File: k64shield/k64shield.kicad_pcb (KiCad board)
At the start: 2 copper layers, 7 parts, among them J1 top_left_header_02x08, J2 bottom_left_header_02x06, J3 rpi_motor_driver_header, J4 top_right_header_02x10, J5 bottom_right_header_02x08, J6 camera_header_01x05, J7 servo_header_01x03

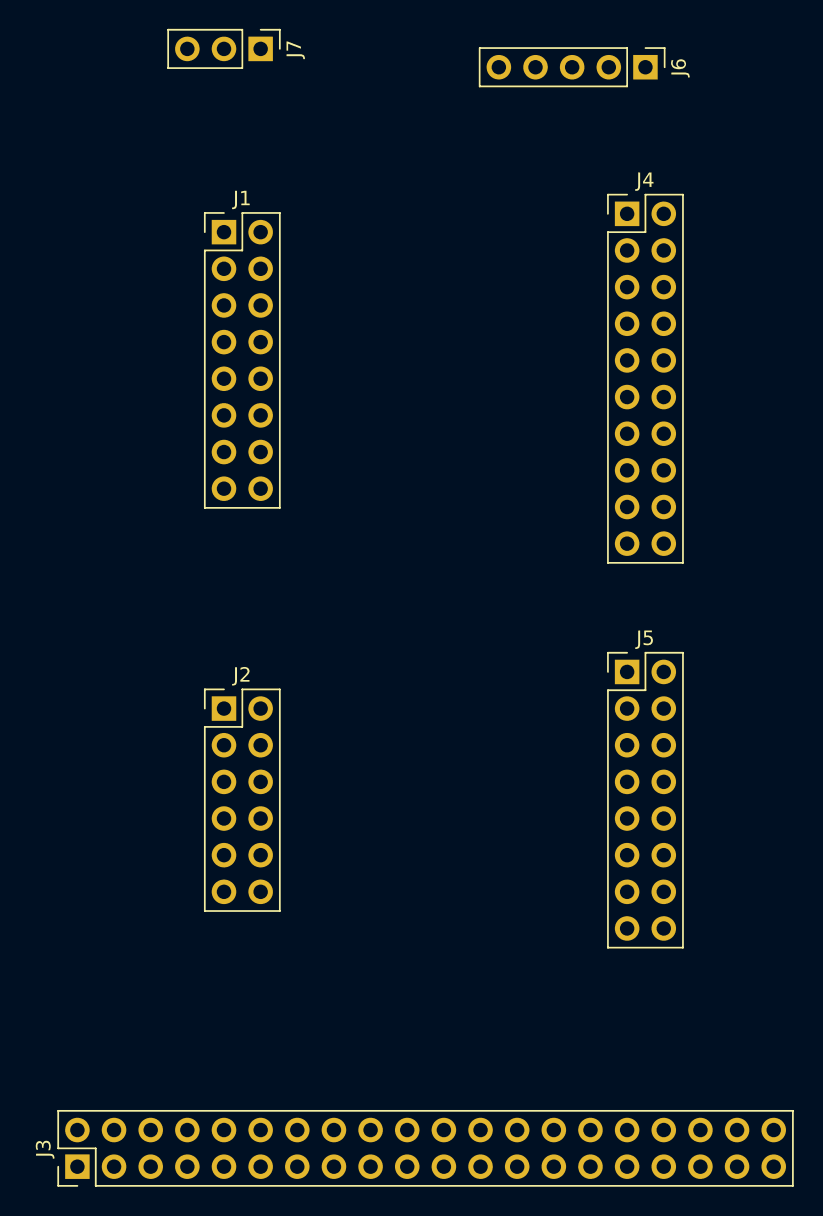
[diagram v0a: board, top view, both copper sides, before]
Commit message: Some of the PCB completed
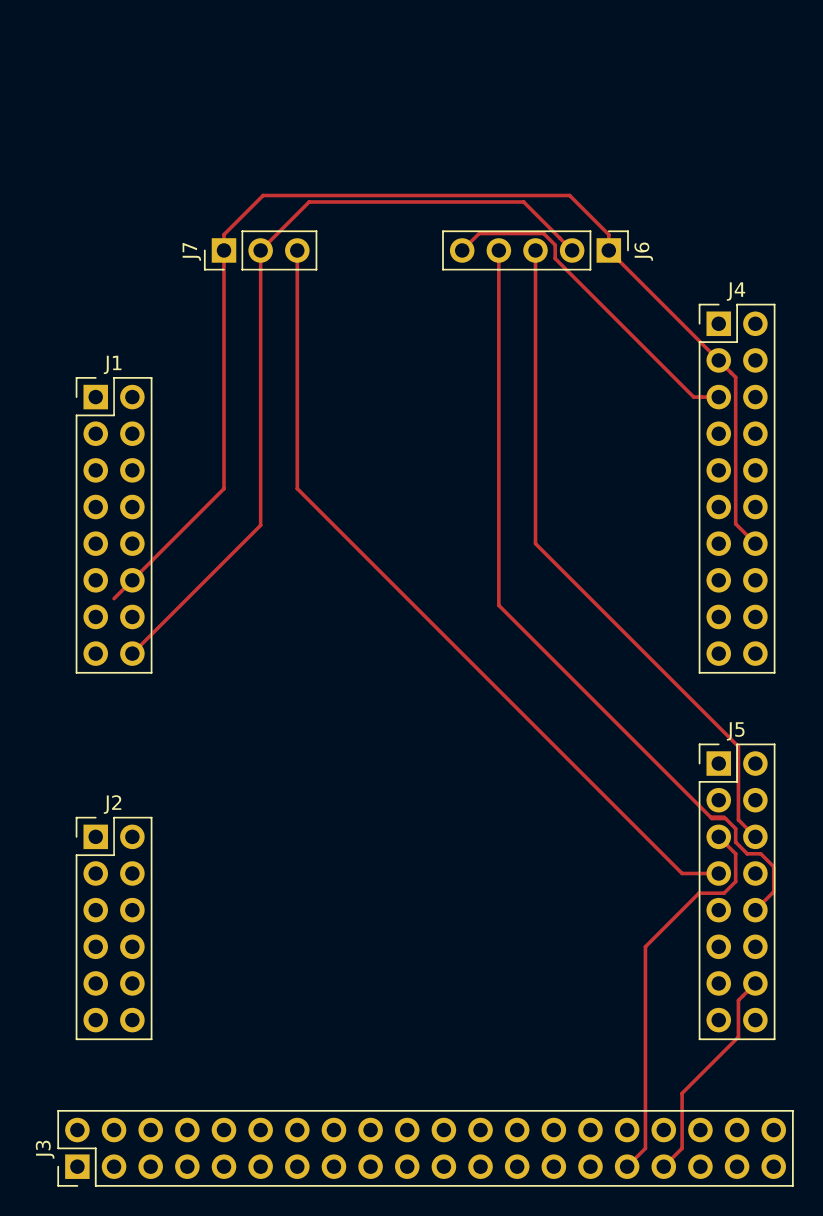
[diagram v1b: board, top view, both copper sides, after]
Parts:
- moved J1 14.5 mm to (104.1, 72.4)
- moved J7 14.2 mm to (113.0, 62.2), turned to 90 degrees
- moved J6 13.0 mm to (139.7, 62.2)
- moved J2 12.6 mm to (104.1, 102.9)
- moved J4 9.92 mm to (147.3, 67.3)
- moved J5 8.98 mm to (147.3, 97.8)
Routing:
- net /GND: track 0.00 -> 82.9 mm
- net /SIG: track 0.00 -> 56.8 mm
- net /SI: track 0.00 -> 56.2 mm
- net /5V: track 0.00 -> 56.0 mm
- net /CLK: track 0.00 -> 47.0 mm
- net /A1: track 0.00 -> 27.5 mm
- net /AO: track 0.00 -> 23.5 mm
- net /A2: track 0.00 -> 15.3 mm
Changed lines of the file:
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@@
-(kicad_pcb (version 4) (host pcbnew 4.0.7)
+(kicad_pcb (version 20171130) (host pcbnew 5.0.1-33cea8e~68~ubuntu18.04.1)
   (general
-    (links 25)
-    (no_connects 25)
-    (area 0 0 0 0)
     (thickness 1.6)
     (drawings 0)
-    (tracks 0)
+    (tracks 57)
     (zones 0)
     (modules 7)
@@
     (pad_drill 0.762)
     (pad_to_mask_clearance 0.2)
+    (solder_mask_min_width 0.25)
     (aux_axis_origin 0 0)
     (visible_elements FFFFFF7F)
@@
       (layerselection 0x00030_80000001)
       (usegerberextensions false)
+      (usegerberattributes false)
+      (usegerberadvancedattributes false)
+      (creategerberjobfile false)
       (excludeedgelayer true)
       (linewidth 0.100000)
@@
       (hpglpennumber 1)
       (hpglpenspeed 20)
-      (hpglpendiameter 15)
-      (hpglpenoverlay 2)
+      (hpglpendiameter 15.000000)
       (psnegative false)
       (psa4output false)
@@
   )
   (module Pin_Headers:Pin_Header_Straight_2x08_Pitch2.54mm (layer F.Cu)
-    (at 113.03 60.96)
+    (at 104.14 72.39)
     (descr "Through hole straight pin header, 2x08, 2.54mm pitch, double rows")
     (tags "Through hole pin header THT 2x08 2.54mm double row")
@@
   )
   (module Pin_Headers:Pin_Header_Straight_2x06_Pitch2.54mm (layer F.Cu)
-    (at 113.03 93.98)
+    (at 104.14 102.87)
     (descr "Through hole straight pin header, 2x06, 2.54mm pitch, double rows")
     (tags "Through hole pin header THT 2x06 2.54mm double row")
@@
   )
   (module Pin_Headers:Pin_Header_Straight_2x10_Pitch2.54mm (layer F.Cu)
-    (at 140.97 59.69)
+    (at 147.32 67.31)
     (descr "Through hole straight pin header, 2x10, 2.54mm pitch, double rows")
     (tags "Through hole pin header THT 2x10 2.54mm double row")
@@
   )
   (module Pin_Headers:Pin_Header_Straight_2x08_Pitch2.54mm (layer F.Cu)
-    (at 140.97 91.44)
+    (at 147.32 97.79)
     (descr "Through hole straight pin header, 2x08, 2.54mm pitch, double rows")
     (tags "Through hole pin header THT 2x08 2.54mm double row")
@@
   )
   (module Pin_Headers:Pin_Header_Straight_1x05_Pitch2.54mm (layer F.Cu)
-    (at 142.24 49.53 270)
+    (at 139.7 62.23 270)
     (descr "Through hole straight pin header, 1x05, 2.54mm pitch, single row")
     (tags "Through hole pin header THT 1x05 2.54mm single row")
@@
     (fp_line (start 1.8 11.95) (end 1.8 -1.8) (layer F.CrtYd) (width 0.05))
     (fp_line (start 1.8 -1.8) (end -1.8 -1.8) (layer F.CrtYd) (width 0.05))
-    (fp_text user %R (at 0 5.08 360) (layer F.Fab)
+    (fp_text user %R (at 0 5.08) (layer F.Fab)
       (effects (font (size 1 1) (thickness 0.15)))
     )
@@
   )
   (module Pin_Headers:Pin_Header_Straight_1x03_Pitch2.54mm (layer F.Cu)
-    (at 115.57 48.26 270)
+    (at 113.03 62.23 90)
     (descr "Through hole straight pin header, 1x03, 2.54mm pitch, single row")
     (tags "Through hole pin header THT 1x03 2.54mm single row")
-    (fp_text reference J7 (at 0 -2.33 270) (layer F.SilkS)
-      (effects (font (size 1 1) (thickness 0.15)))
-    )
-    (fp_text value servo_header_01x03 (at 0 7.41 270) (layer F.Fab)
+    (fp_text reference J7 (at 0 -2.33 90) (layer F.SilkS)
+      (effects (font (size 1 1) (thickness 0.15)))
+    )
+    (fp_text value servo_header_01x03 (at 0 7.41 90) (layer F.Fab)
       (effects (font (size 1 1) (thickness 0.15)))
     )
@@
     (fp_line (start 1.8 6.85) (end 1.8 -1.8) (layer F.CrtYd) (width 0.05))
     (fp_line (start 1.8 -1.8) (end -1.8 -1.8) (layer F.CrtYd) (width 0.05))
-    (fp_text user %R (at 0 2.54 360) (layer F.Fab)
-      (effects (font (size 1 1) (thickness 0.15)))
-    )
-    (pad 1 thru_hole rect (at 0 0 270) (size 1.7 1.7) (drill 1) (layers *.Cu *.Mask)
-      (net 12 /GND))
-    (pad 2 thru_hole oval (at 0 2.54 270) (size 1.7 1.7) (drill 1) (layers *.Cu *.Mask)
+    (fp_text user %R (at 0 2.54 -180) (layer F.Fab)
+      (effects (font (size 1 1) (thickness 0.15)))
+    )
+    (pad 1 thru_hole rect (at 0 0 90) (size 1.7 1.7) (drill 1) (layers *.Cu *.Mask)
+      (net 12 /GND))
+    (pad 2 thru_hole oval (at 0 2.54 90) (size 1.7 1.7) (drill 1) (layers *.Cu *.Mask)
       (net 15 /5V))
-    (pad 3 thru_hole oval (at 0 5.08 270) (size 1.7 1.7) (drill 1) (layers *.Cu *.Mask)
+    (pad 3 thru_hole oval (at 0 5.08 90) (size 1.7 1.7) (drill 1) (layers *.Cu *.Mask)
       (net 80 /SIG))
     (model ${KISYS3DMOD}/Pin_Headers.3dshapes/Pin_Header_Straight_1x03_Pitch2.54mm.wrl
@@
     )
   )
+  (segment (start 148.169999 70.699999) (end 147.32 69.85) (width 0.25) (layer F.Cu) (net 12))
+  (segment (start 148.495001 71.025001) (end 148.169999 70.699999) (width 0.25) (layer F.Cu) (net 12))
+  (segment (start 148.495001 81.185001) (end 148.495001 71.025001) (width 0.25) (layer F.Cu) (net 12))
+  (segment (start 149.86 82.55) (end 148.495001 81.185001) (width 0.25) (layer F.Cu) (net 12))
+  (segment (start 147.32 69.85) (end 139.7 62.23) (width 0.25) (layer F.Cu) (net 12))
+  (segment (start 113.03 78.74) (end 113.03 62.23) (width 0.25) (layer F.Cu) (net 12))
+  (segment (start 106.68 85.09) (end 113.03 78.74) (width 0.25) (layer F.Cu) (net 12))
+  (segment (start 139.7 61.13) (end 136.99 58.42) (width 0.25) (layer F.Cu) (net 12))
+  (segment (start 139.7 62.23) (end 139.7 61.13) (width 0.25) (layer F.Cu) (net 12))
+  (segment (start 113.03 61.13) (end 113.03 62.23) (width 0.25) (layer F.Cu) (net 12))
+  (segment (start 115.74 58.42) (end 113.03 61.13) (width 0.25) (layer F.Cu) (net 12))
+  (segment (start 136.99 58.42) (end 115.74 58.42) (width 0.25) (layer F.Cu) (net 12))
+  (segment (start 106.68 85.09) (end 105.41 86.36) (width 0.25) (layer F.Cu) (net 12))
+  (segment (start 115.57 81.28) (end 115.57 62.23) (width 0.25) (layer F.Cu) (net 15))
+  (segment (start 106.68 90.17) (end 115.57 81.28) (width 0.25) (layer F.Cu) (net 15))
+  (segment (start 136.310001 61.380001) (end 137.16 62.23) (width 0.25) (layer F.Cu) (net 15))
+  (segment (start 133.80001 58.87001) (end 136.310001 61.380001) (width 0.25) (layer F.Cu) (net 15))
+  (segment (start 118.92999 58.87001) (end 133.80001 58.87001) (width 0.25) (layer F.Cu) (net 15))
+  (segment (start 115.57 62.23) (end 118.92999 58.87001) (width 0.25) (layer F.Cu) (net 15))
+  (segment (start 147.694003 106.774999) (end 145.955001 106.774999) (width 0.25) (layer F.Cu) (net 50))
+  (segment (start 148.495001 105.974001) (end 147.694003 106.774999) (width 0.25) (layer F.Cu) (net 50))
+  (segment (start 147.32 102.87) (end 148.495001 104.045001) (width 0.25) (layer F.Cu) (net 50))
+  (segment (start 148.495001 104.045001) (end 148.495001 105.974001) (width 0.25) (layer F.Cu) (net 50))
+  (segment (start 145.955001 106.774999) (end 142.24 110.49) (width 0.25) (layer F.Cu) (net 50))
+  (segment (start 142.24 124.46) (end 140.97 125.73) (width 0.25) (layer F.Cu) (net 50))
+  (segment (start 142.24 110.49) (end 142.24 124.46) (width 0.25) (layer F.Cu) (net 50))
+  (segment (start 144.78 124.46) (end 144.78 120.65) (width 0.25) (layer F.Cu) (net 52))
+  (segment (start 143.51 125.73) (end 144.78 124.46) (width 0.25) (layer F.Cu) (net 52))
+  (segment (start 149.010001 113.879999) (end 149.86 113.03) (width 0.25) (layer F.Cu) (net 52))
+  (segment (start 148.684999 114.205001) (end 149.010001 113.879999) (width 0.25) (layer F.Cu) (net 52))
+  (segment (start 148.684999 116.745001) (end 148.684999 114.205001) (width 0.25) (layer F.Cu) (net 52))
+  (segment (start 144.78 120.65) (end 148.684999 116.745001) (width 0.25) (layer F.Cu) (net 52))
+  (segment (start 146.117919 72.39) (end 147.32 72.39) (width 0.25) (layer F.Cu) (net 60))
+  (segment (start 145.580998 72.39) (end 146.117919 72.39) (width 0.25) (layer F.Cu) (net 60))
+  (segment (start 135.984999 62.794001) (end 145.580998 72.39) (width 0.25) (layer F.Cu) (net 60))
+  (segment (start 135.984999 61.855997) (end 135.984999 62.794001) (width 0.25) (layer F.Cu) (net 60))
+  (segment (start 135.184001 61.054999) (end 135.984999 61.855997) (width 0.25) (layer F.Cu) (net 60))
+  (segment (start 130.715001 61.054999) (end 135.184001 61.054999) (width 0.25) (layer F.Cu) (net 60))
+  (segment (start 129.54 62.23) (end 130.715001 61.054999) (width 0.25) (layer F.Cu) (net 60))
+  (segment (start 148.684999 101.694999) (end 148.684999 96.614999) (width 0.25) (layer F.Cu) (net 79))
+  (segment (start 149.86 102.87) (end 148.684999 101.694999) (width 0.25) (layer F.Cu) (net 79))
+  (segment (start 134.62 82.55) (end 134.62 62.23) (width 0.25) (layer F.Cu) (net 79))
+  (segment (start 148.684999 96.614999) (end 134.62 82.55) (width 0.25) (layer F.Cu) (net 79))
+  (segment (start 147.32 105.41) (end 144.78 105.41) (width 0.25) (layer F.Cu) (net 80))
+  (segment (start 118.11 78.74) (end 118.11 62.23) (width 0.25) (layer F.Cu) (net 80))
+  (segment (start 144.78 105.41) (end 118.11 78.74) (width 0.25) (layer F.Cu) (net 80))
+  (segment (start 147.694003 101.505001) (end 146.755999 101.505001) (width 0.25) (layer F.Cu) (net 83))
+  (segment (start 132.08 86.829002) (end 132.08 62.23) (width 0.25) (layer F.Cu) (net 83))
+  (segment (start 146.850998 101.6) (end 132.08 86.829002) (width 0.25) (layer F.Cu) (net 83))
+  (segment (start 147.789002 101.6) (end 146.850998 101.6) (width 0.25) (layer F.Cu) (net 83))
+  (segment (start 149.86 107.95) (end 151.13 106.68) (width 0.25) (layer F.Cu) (net 83))
+  (segment (start 148.495001 102.305999) (end 147.789002 101.6) (width 0.25) (layer F.Cu) (net 83))
+  (segment (start 148.495001 103.244003) (end 148.495001 102.305999) (width 0.25) (layer F.Cu) (net 83))
+  (segment (start 149.295999 104.045001) (end 148.495001 103.244003) (width 0.25) (layer F.Cu) (net 83))
+  (segment (start 150.234003 104.045001) (end 149.295999 104.045001) (width 0.25) (layer F.Cu) (net 83))
+  (segment (start 151.13 104.940998) (end 150.234003 104.045001) (width 0.25) (layer F.Cu) (net 83))
+  (segment (start 151.13 106.68) (end 151.13 104.940998) (width 0.25) (layer F.Cu) (net 83))
 )
